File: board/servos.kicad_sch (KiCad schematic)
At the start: 5 parts

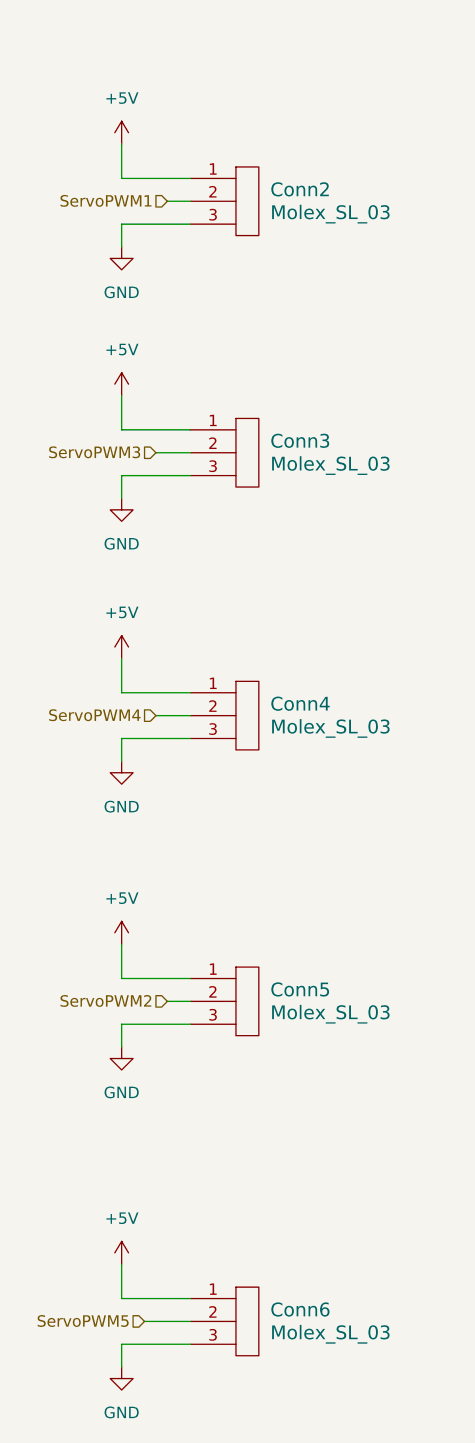
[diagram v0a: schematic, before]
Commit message: Added Servo, cleaned up schematic
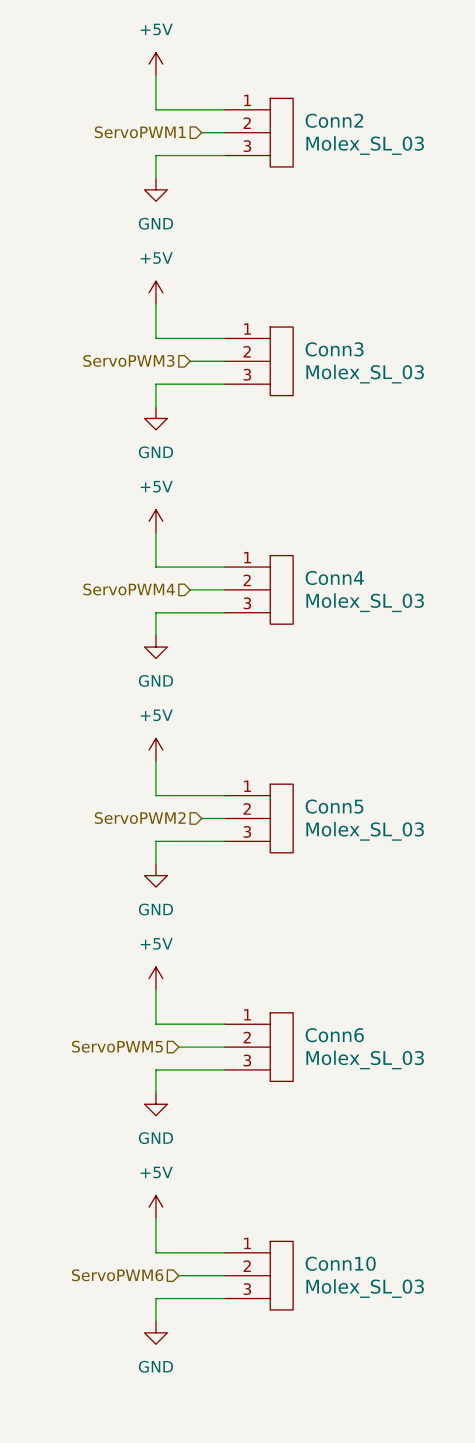
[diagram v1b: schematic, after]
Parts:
- added Conn10: Molex_SL_03, symbol MRDT_Connectors:Molex_SL_03
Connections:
- net +5V: now also Conn10.1
- net GND: now also Conn10.3
- new net ServoPWM6: Conn10.2
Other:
- moved on the sheet: Conn2, Conn3, Conn4, Conn5, Conn6

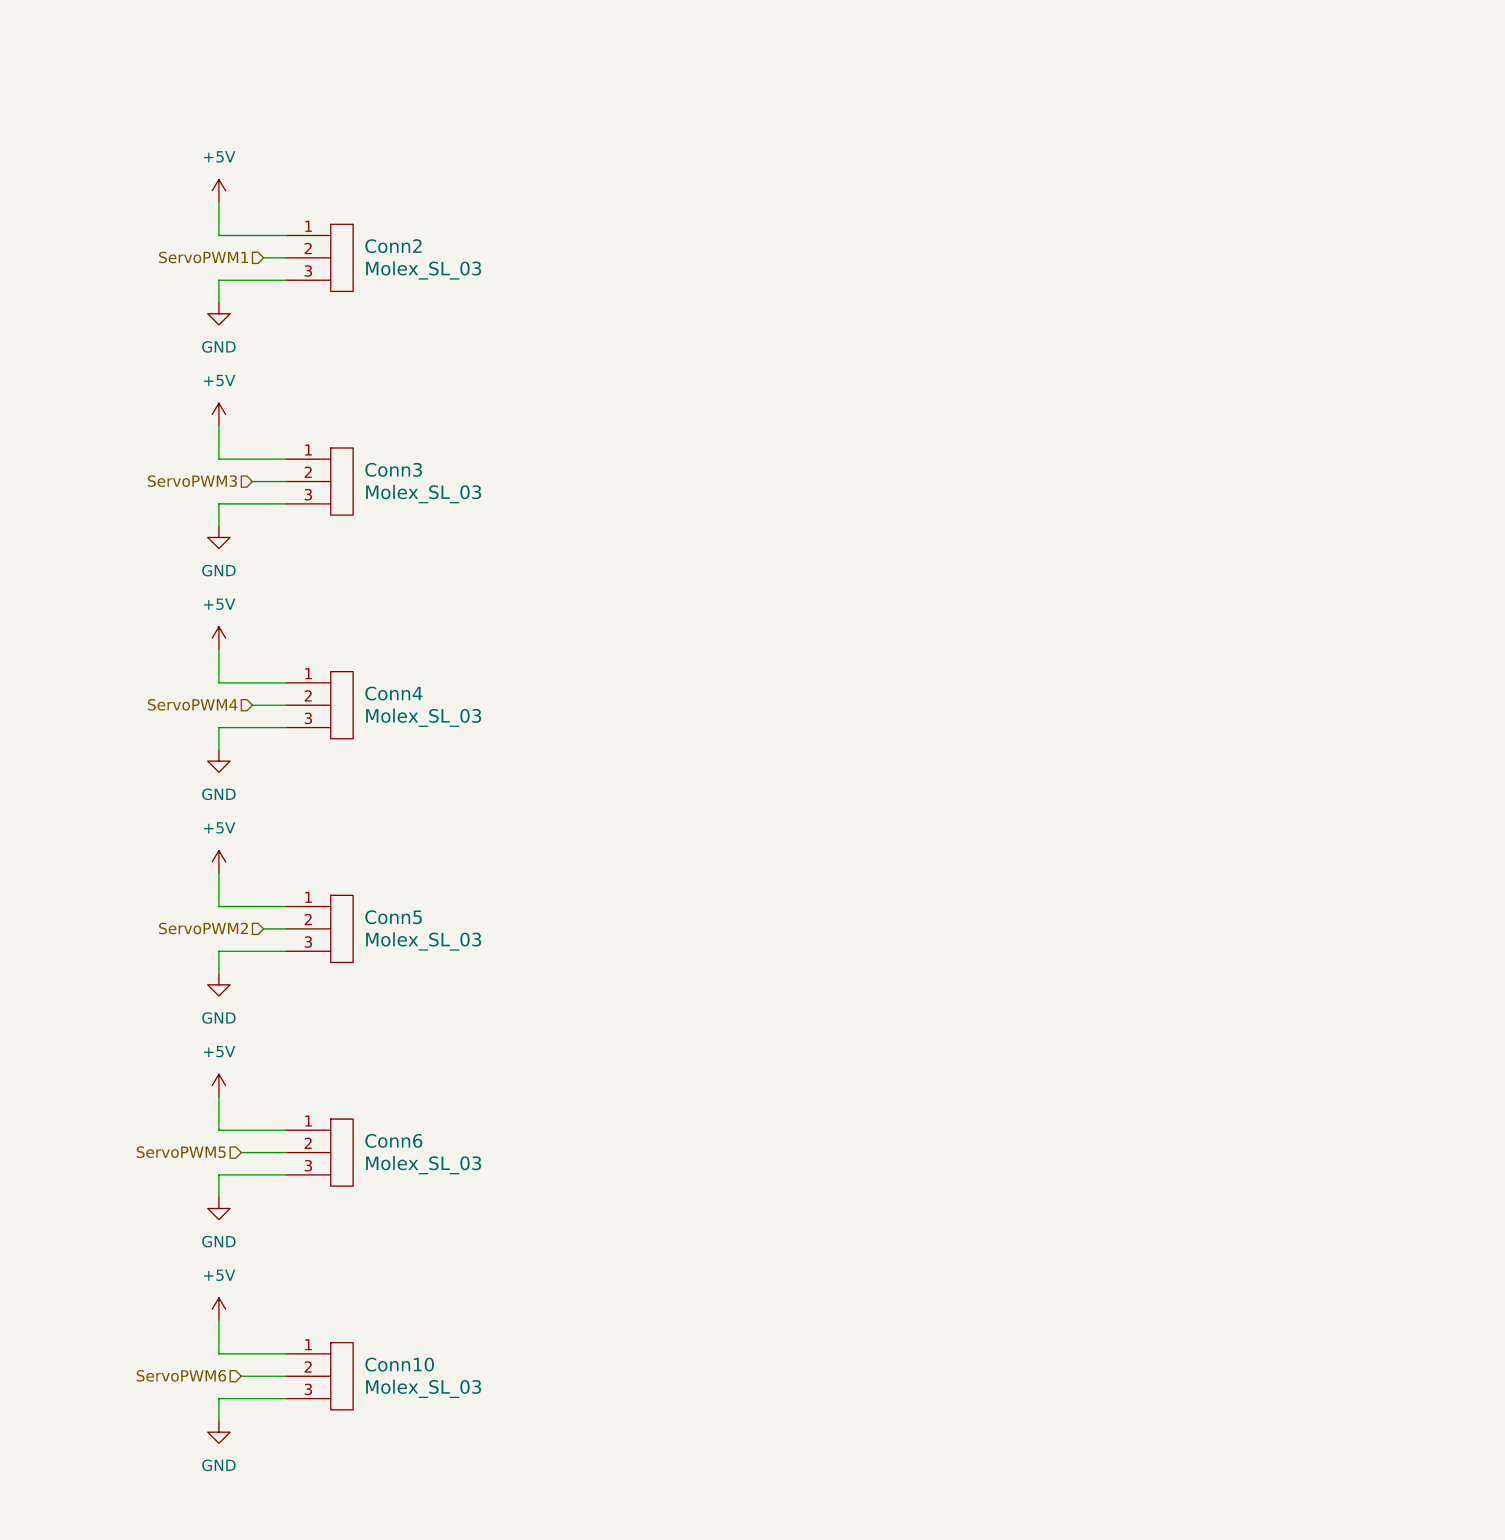
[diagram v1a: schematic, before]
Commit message: Added Labels, Missing Requirements, and Refined Look
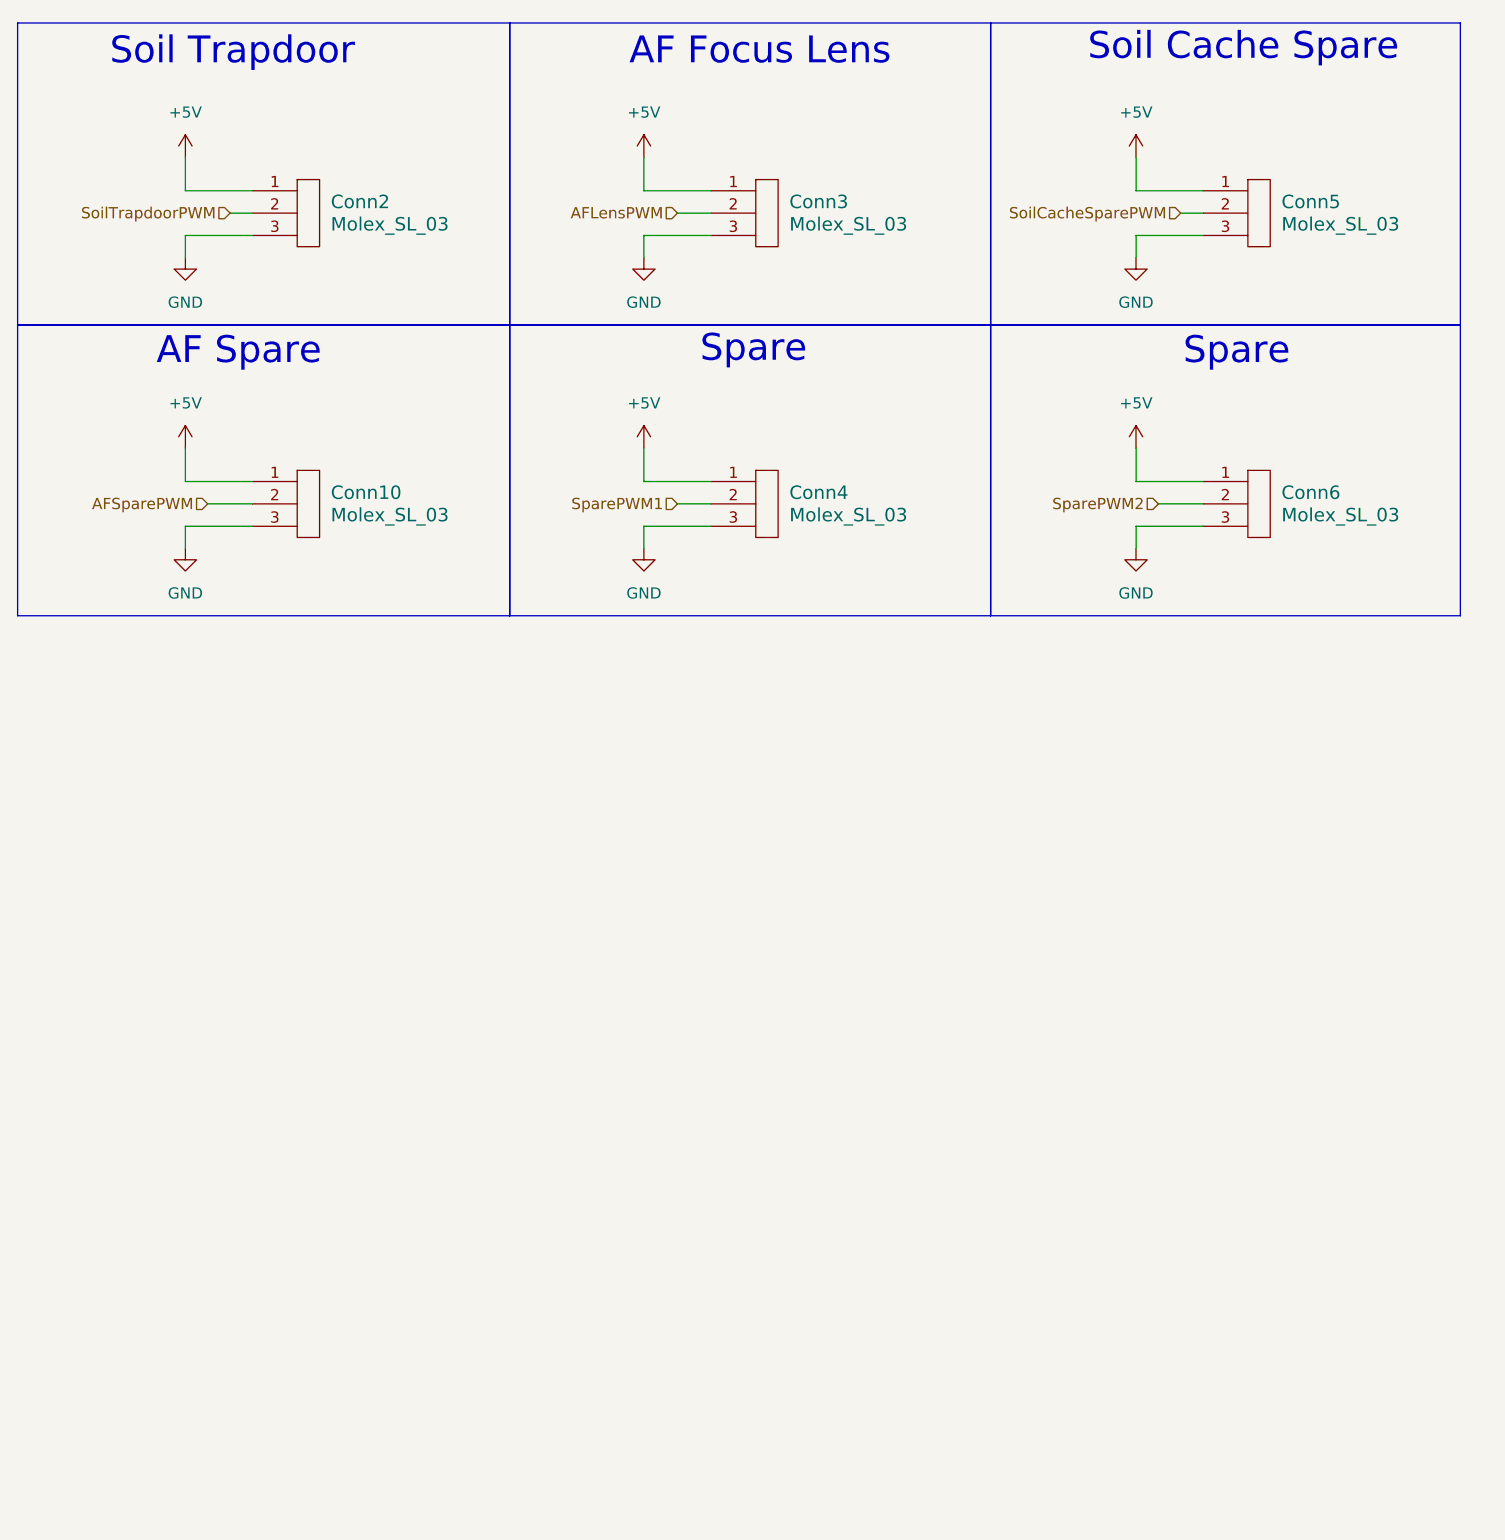
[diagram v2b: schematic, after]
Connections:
- net ServoPWM1 renamed SoilTrapdoorPWM
- net ServoPWM2 renamed SoilCacheSparePWM
- net ServoPWM3 renamed AFLensPWM
- net ServoPWM4 renamed SparePWM1
- net ServoPWM5 renamed SparePWM2
- net ServoPWM6 renamed AFSparePWM
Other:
- note added: "AF Focus Lens"
- note added: "AF Spare"
- note added: "Soil Cache Spare"
- note added: "Soil Trapdoor"
- note added: "Spare"
- moved on the sheet: Conn10, Conn2, Conn3, Conn4, Conn5, Conn6

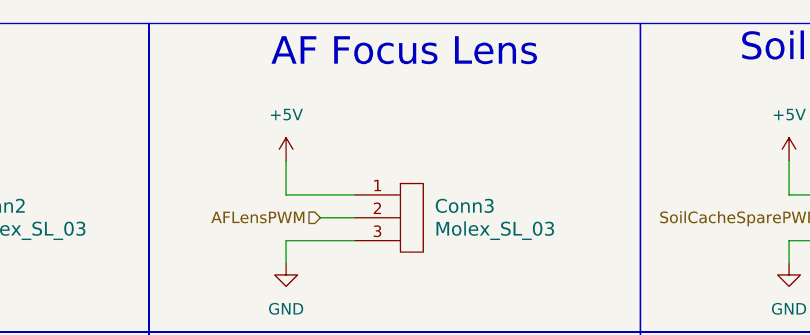
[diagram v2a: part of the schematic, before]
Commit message: Adjusted resistor values & renamed AF outputs
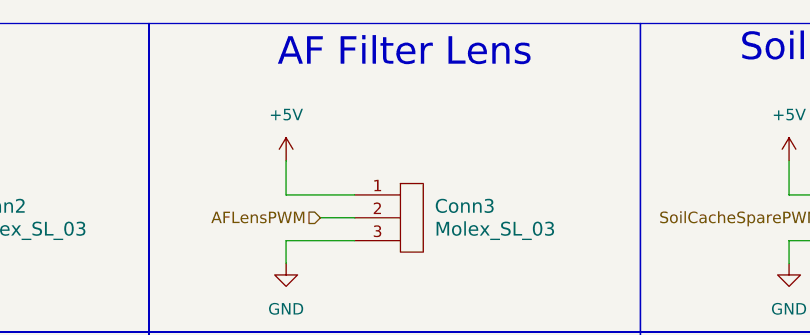
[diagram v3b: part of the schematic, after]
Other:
- note added: "AF Filter Lens"
- note removed: "AF Focus Lens"
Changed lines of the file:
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@@
 		)
 	)
-	(text "AF Focus Lens"
+	(text "AF Filter Lens"
 		(exclude_from_sim no)
 		(at 97.028 16.002 0)

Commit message: assigned footprints
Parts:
- Conn10, Conn2, Conn3, Conn4, Conn5, Conn6: footprint (none) -> MRDT_Connectors:MOLEX_SL_03_Vertical
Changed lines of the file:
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@@
 			)
 		)
-		(property "Footprint" ""
+		(property "Footprint" "MRDT_Connectors:MOLEX_SL_03_Vertical"
 			(at 44.45 38.1 0)
 			(effects
@@
 			)
 		)
-		(property "Footprint" ""
+		(property "Footprint" "MRDT_Connectors:MOLEX_SL_03_Vertical"
 			(at 152.4 38.1 0)
 			(effects
@@
 			)
 		)
-		(property "Footprint" ""
+		(property "Footprint" "MRDT_Connectors:MOLEX_SL_03_Vertical"
 			(at 44.45 71.12 0)
 			(effects
@@
 			)
 		)
-		(property "Footprint" ""
+		(property "Footprint" "MRDT_Connectors:MOLEX_SL_03_Vertical"
 			(at 152.4 71.12 0)
 			(effects
@@
 			)
 		)
-		(property "Footprint" ""
+		(property "Footprint" "MRDT_Connectors:MOLEX_SL_03_Vertical"
 			(at 96.52 38.1 0)
 			(effects
@@
 			)
 		)
-		(property "Footprint" ""
+		(property "Footprint" "MRDT_Connectors:MOLEX_SL_03_Vertical"
 			(at 96.52 71.12 0)
 			(effects

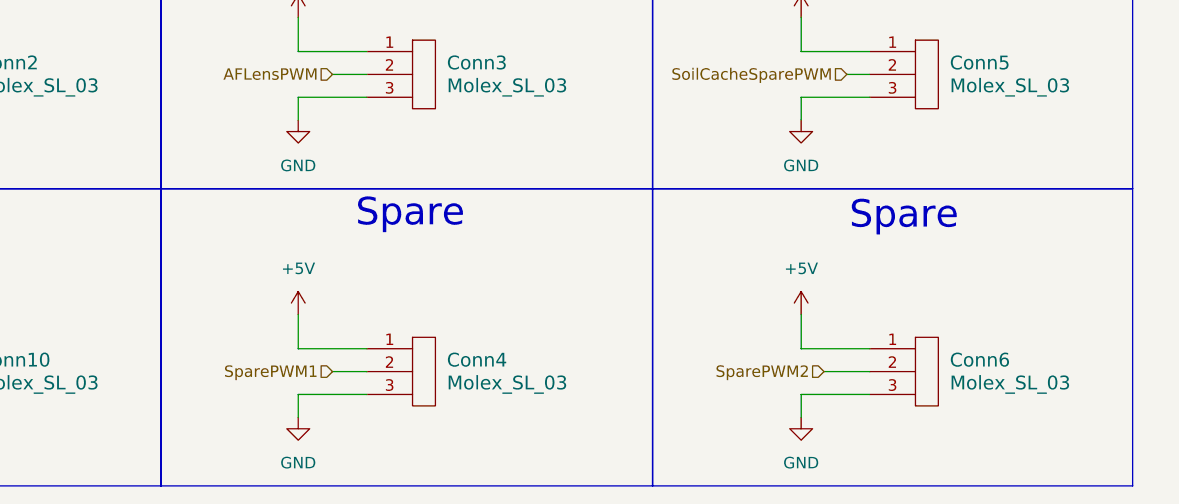
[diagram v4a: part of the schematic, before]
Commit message: added pin for AF, added gimbal names, refined look
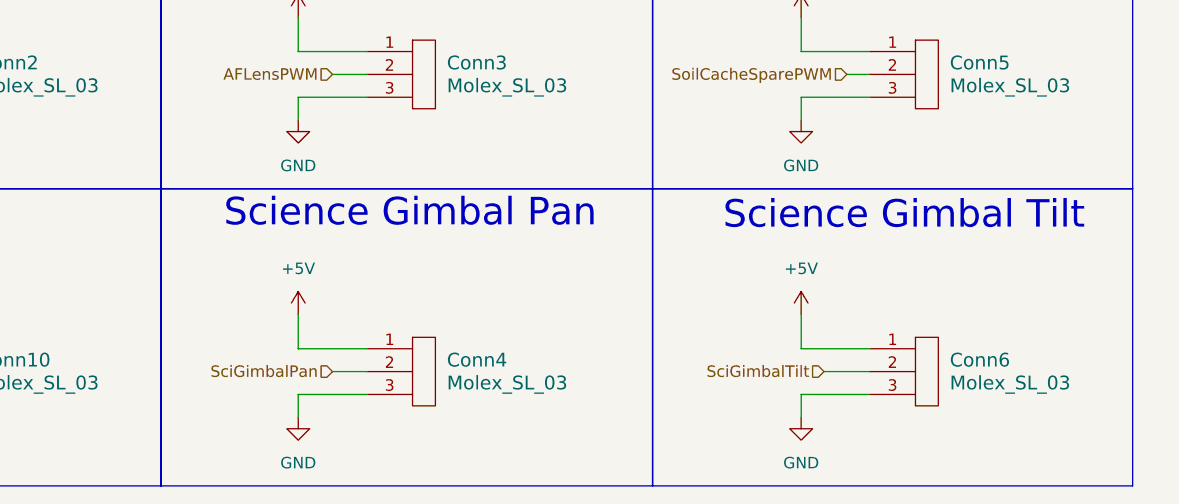
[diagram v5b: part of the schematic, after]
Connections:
- net SparePWM1 renamed SciGimbalPan
- net SparePWM2 renamed SciGimbalTilt
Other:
- note added: "Science Gimbal Pan"
- note added: "Science Gimbal Tilt"
- note removed: "Spare"
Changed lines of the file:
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@@
 		)
 	)
-	(text "Spare"
+	(text "Science Gimbal Pan"
 		(exclude_from_sim no)
 		(at 96.266 49.784 0)
@@
 		)
 	)
-	(text "Spare"
+	(text "Science Gimbal Tilt"
 		(exclude_from_sim no)
 		(at 151.13 50.038 0)
@@
 		)
 	)
-	(hierarchical_label "SparePWM2"
+	(hierarchical_label "SciGimbalTilt"
 		(shape input)
 		(at 142.24 67.31 180)
@@
 		)
 	)
-	(hierarchical_label "SparePWM1"
+	(hierarchical_label "SciGimbalPan"
 		(shape input)
 		(at 87.63 67.31 180)

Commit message: Redesigning Layout
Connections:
- net AFSparePWM renamed SparePWM1
- net SoilCacheSparePWM renamed SparePWM2
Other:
- note added: "Spare Servo 1"
- note added: "Spare Servo 2"
- note removed: "AF Spare"
- note removed: "Soil Cache Spare"
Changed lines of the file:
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@@
 		)
 	)
-	(text "AF Spare"
+	(text "Spare Servo 1"
 		(exclude_from_sim no)
 		(at 37.846 50.038 0)
@@
 		)
 	)
-	(text "Soil Cache Spare"
+	(text "Spare Servo 2"
 		(exclude_from_sim no)
 		(at 151.892 15.494 0)
@@
 		)
 	)
-	(hierarchical_label "AFSparePWM"
+	(hierarchical_label "SparePWM1"
 		(shape input)
 		(at 34.29 67.31 180)
@@
 		)
 	)
-	(hierarchical_label "SoilCacheSparePWM"
+	(hierarchical_label "SparePWM2"
 		(shape input)
 		(at 144.78 34.29 180)
